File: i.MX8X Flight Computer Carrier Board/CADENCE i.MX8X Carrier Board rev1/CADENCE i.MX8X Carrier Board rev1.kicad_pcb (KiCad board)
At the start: 6 copper layers, 167.7 x 85 mm, 431 parts, among them CN1 DF11-16DP-2DSA(08), CN2 DF11-16DP-2DSA(08), CN3 DF11-16DP-2DSA(08), CN4 DF11-16DP-2DSA(08), J1 BTH-070-02-L-D-A, J10 Conn_01x04, J11 Conn_01x04, J16 Conn_01x04, J17 Conn_01x04, J2 USB_C_Receptacle_USB2.0_16P, J21 Conn_02x02_Odd_Even, J22 Conn_01x04, J3 USB_A, J4 Conn_Coaxial, J5 USB_C_Receptacle_USB2.0_16P, J6 Conn_01x01, J7 Conn_01x08, J8 Conn_02x26_Odd_Even, J9 Conn_02x26_Odd_Even, Q1 IRLML6401, Q2 BSS138, Q3 BSS138, SW1 SW_DIP_x01, SW2 KMR221GLFS, SW3 SW_DIP_x04, SW4 SW_DIP_x01, T1 WE-RJ45_7499111121A, T2 WE-RJ45_7499111121A, U1 LT8612, U10 ZDSD04GLGEAG, U11 MR20H40, U12 MR20H40, U13 DP83867IRRGZR, U14 74LVC2G07, U15 USBLC6-2SC6, U16 USBLC6-2SC6, U17 SN65C1168ERGYR, U18 P82B715DR, U19 P82B715DR, U2 LT8612, U20 P82B715DR, U21 INA219AxDCN, U22 Skytraq Orion B16 GPS, U23 RV-3028-C7, U24 LSM6DSO, U25 LIS2MDL, U26 TMP112xxDRL, U27 INA219AxDCN, U28 LP38693MP-ADJ/NOPB, U29 74CBTLV3257BQ, U3 TPS22975, U30 CAT93C66VI-GT3, U31 USBLC6-2SC6, U32 FT2232HL, U33 SN65HVD233, U34 INA219AxDCN, U35 TPS22810DBV, U36 INA219AxDCN, U37 TPS22810DBV, U38 INA219AxDCN, U39 TPS22975, U4 LT3115-1, U40 TXS0101DCKR, U41 TXS0101DCKR, U5 TLV71325PDQNR, U6 TLV71310PDQNR, U7 TLV1704, U8 BD2204GUL-E2, U9 MX25UM51245G, Y1 25MHz, Y2 12MHz

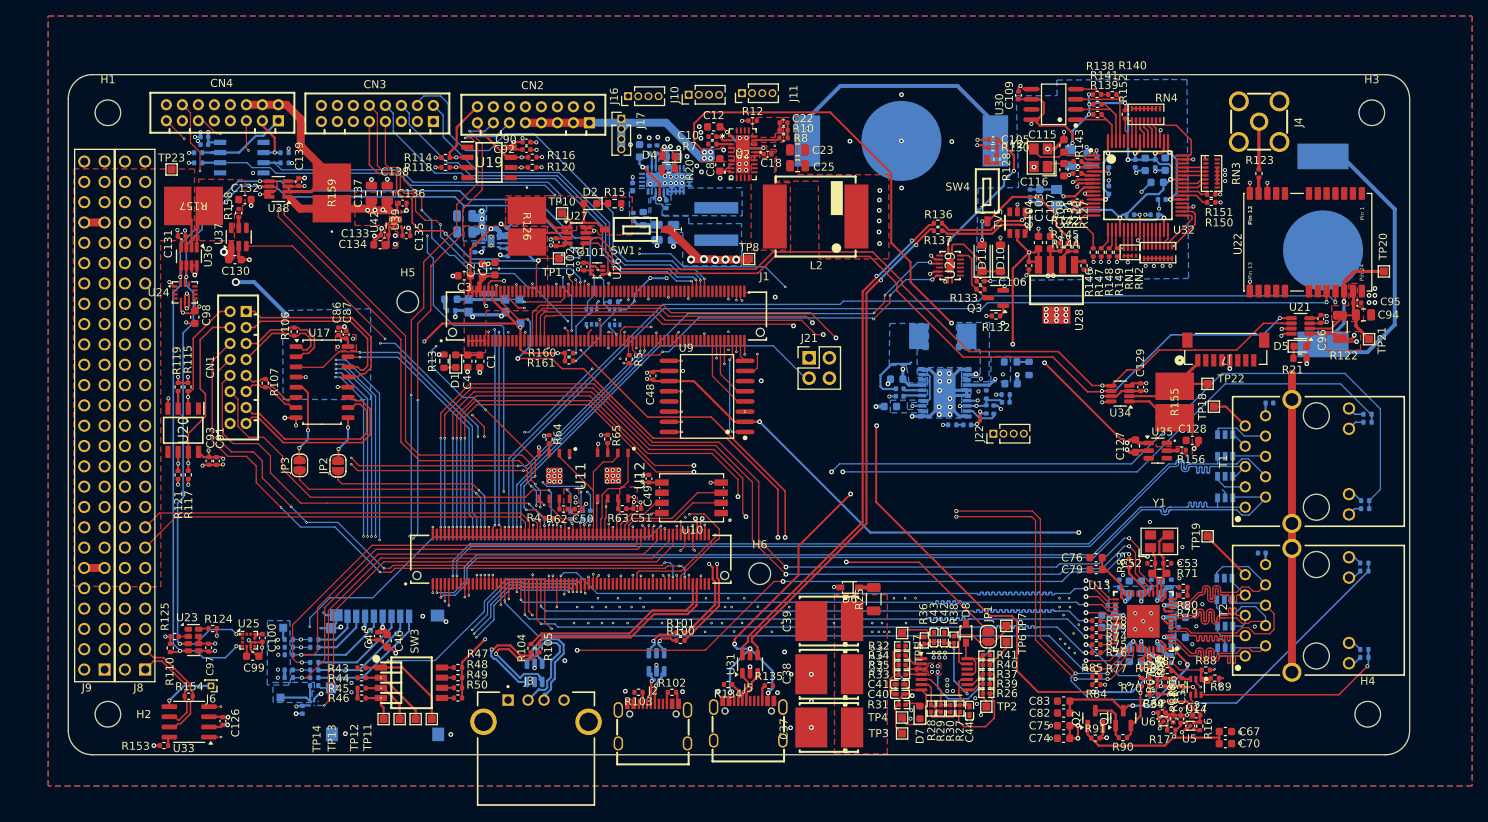
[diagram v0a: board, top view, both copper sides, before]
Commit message: Preliminary Final Changes
- Satnogs connector mounting holes adjusted
- length of pcb +5mm to left
fixed drc errors:
- solder mask expansions, footprint clearance for tlv713p, connections with issues, missing connections, minor adjustments to some traces
- double checked BOM filled with components in stock on jlcpcb
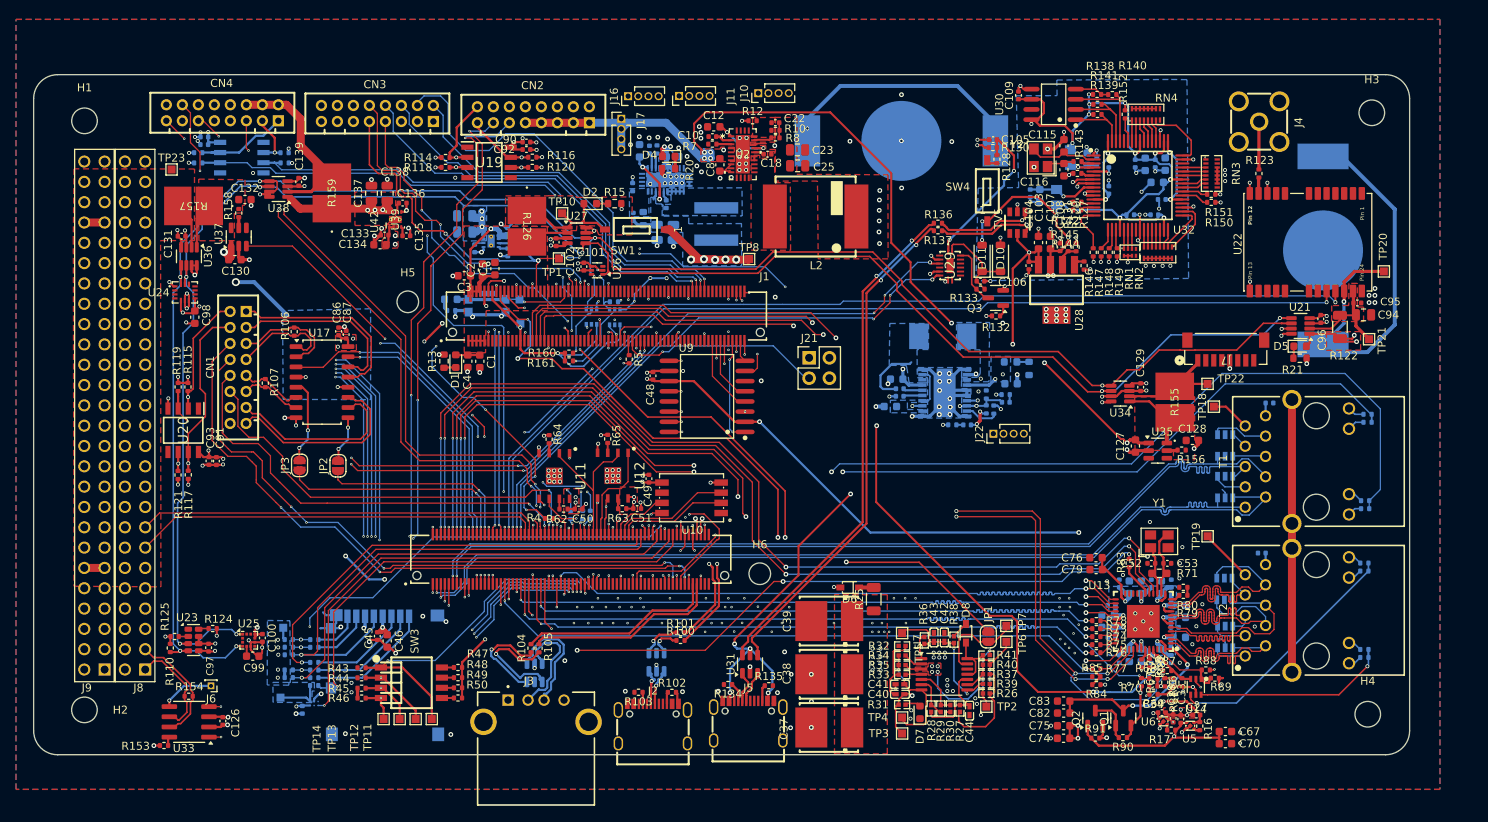
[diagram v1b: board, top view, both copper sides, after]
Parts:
- moved J10 8.70 mm to (306.3, 68.2)
- moved J11 7.87 mm to (296.4, 68.5)
- moved H1 3.09 mm to (222.1, 71.6)
- moved H2 2.98 mm to (222.1, 145.2)
- moved C22 1.02 mm to (308.5, 71.8)
- moved R8 1.01 mm to (308.5, 73.8)
- moved R10 1.01 mm to (308.5, 72.8)
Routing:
- net P_1V8_OUT: track 198.3 -> 237.5 mm, vias 18 -> 21
- net GPIO4_IO20: track 96.6 -> 92.2 mm
- net /External Board Connections/IMAGER_PWR_MONITOR: track 6.52 -> 10.1 mm
- net GNDPWR: track 37.3 -> 34.1 mm
- net P_3V3: track 34.5 -> 36.5 mm
- net +3.3V: track 108.7 -> 110.6 mm, vias 51 -> 52
- net +5V: track 142.4 -> 143.9 mm
- net Net-(U7C-+): track 2.50 -> 3.70 mm
- net 3V3_FTDI: track 105.8 -> 104.6 mm, vias 19 -> 18
- net /Power/5V FB: track 0.95 -> 0.00 mm
- net 5V Power Good: track 3.27 -> 2.32 mm
- net Net-(U41-OE): track 8.79 -> 9.30 mm
- net HS_I2C0_SDA: track 248.6 -> 248.4 mm, vias 8 -> 9
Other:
- board size 167.7 x 85 mm -> 172 x 85 mm
- board text removed: "Corner center from width end of each satnogs connector to other is 10.030mm"
